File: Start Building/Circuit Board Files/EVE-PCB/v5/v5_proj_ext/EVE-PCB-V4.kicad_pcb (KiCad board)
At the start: 4 copper layers, 199.5 x 49.7 mm, 8 parts, among them J1 Conn_02x09_Top_Bottom, J2 Conn_02x09_Top_Bottom, J3 Conn_02x09_Top_Bottom, J4 Conn_02x09_Top_Bottom, J6 Conn_02x18_Odd_Even, J7 Conn_02x22_Odd_Even

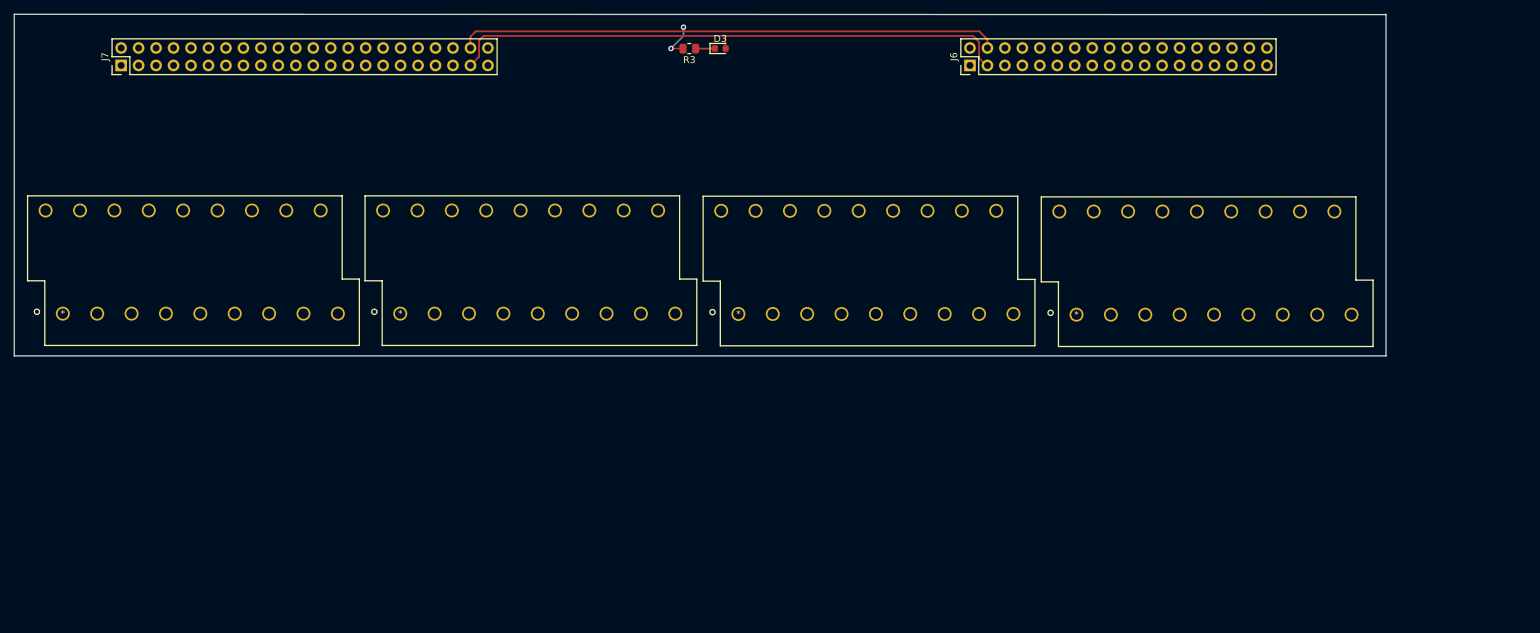
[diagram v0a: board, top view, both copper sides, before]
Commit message: PCBv5 update some schematics
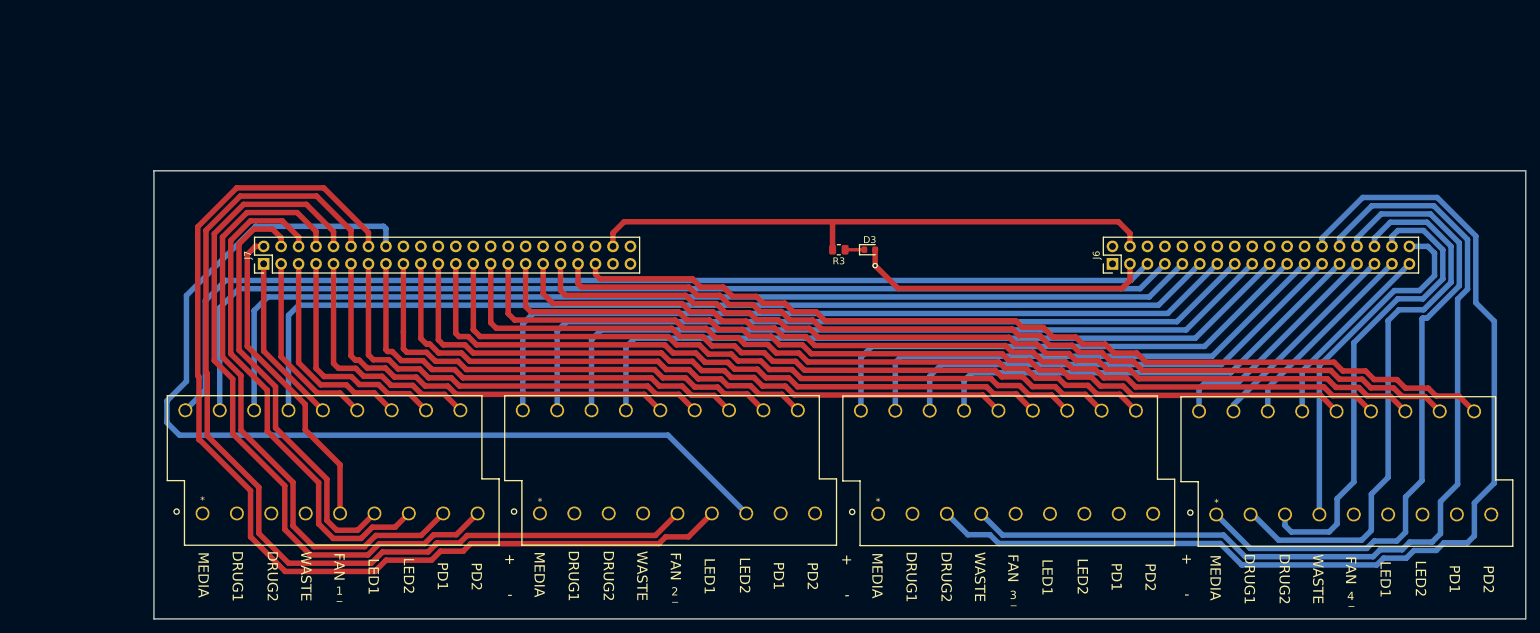
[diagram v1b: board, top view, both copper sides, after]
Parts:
- moved R3 36.5 mm to (150.0, 65.5)
- moved D3 36.5 mm to (154.5, 65.5)
- moved J7 35.5 mm to (66.4, 67.6)
- moved J6 35.5 mm to (189.8, 67.6)
- moved J2 35.5 mm to (155.8, 103.9)
- moved J3 35.5 mm to (106.6, 103.9)
- moved J1 35.5 mm to (57.5, 103.9)
- moved J4 35.5 mm to (204.9, 104.0)
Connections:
- J1 pad 1: /MEDIA1_POS -> /MEDIA1_NEG
- J1 pad 10: /MEDIA1_NEG -> /MEDIA1_POS
- J1 pad 11: /DRUG11_NEG -> /DRUG11_POS
- J1 pad 12: /DRUG12_NEG -> /DRUG12_POS
- J1 pad 13: /WASTE1_NEG -> /WASTE1_POS
- J1 pad 14: /FAN1_NEG -> /FAN1_POS
- J1 pad 15: /LED11_NEG -> /LED11_POS
- J1 pad 16: /LED12_NEG -> /LED12_POS
- J1 pad 17: /PD11_NEG -> /PD11_POS
- J1 pad 18: /PD12_NEG -> /PD12_POS
- J1 pad 2: /DRUG11_POS -> /DRUG11_NEG
- J1 pad 3: /DRUG12_POS -> /DRUG12_NEG
- J1 pad 4: /WASTE1_POS -> /WASTE1_NEG
- J1 pad 5: /FAN1_POS -> /FAN1_NEG
- J1 pad 6: /LED11_POS -> /LED11_NEG
- J1 pad 7: /LED12_POS -> /LED12_NEG
- J1 pad 8: /PD11_POS -> /PD11_NEG
- J1 pad 9: /PD12_POS -> /PD12_NEG
- J2 pad 1: /MEDIA3_POS -> /MEDIA3_NEG
- J2 pad 10: /MEDIA3_NEG -> /MEDIA3_POS
- J2 pad 11: /DRUG31_NEG -> /DRUG31_POS
- J2 pad 12: /DRUG32_NEG -> /DRUG32_POS
- J2 pad 13: /WASTE3_NEG -> /WASTE3_POS
- J2 pad 14: /FAN3_NEG -> /FAN3_POS
- J2 pad 15: /LED31_NEG -> /LED31_POS
- J2 pad 16: /LED32_NEG -> /LED32_POS
- J2 pad 17: /PD31_NEG -> /PD31_POS
- J2 pad 18: /PD32_NEG -> /PD32_POS
- J2 pad 2: /DRUG31_POS -> /DRUG31_NEG
- J2 pad 3: /DRUG32_POS -> /DRUG32_NEG
- J2 pad 4: /WASTE3_POS -> /WASTE3_NEG
- J2 pad 5: /FAN3_POS -> /FAN3_NEG
- J2 pad 6: /LED31_POS -> /LED31_NEG
- J2 pad 7: /LED32_POS -> /LED32_NEG
- J2 pad 8: /PD31_POS -> /PD31_NEG
- J2 pad 9: /PD32_POS -> /PD32_NEG
- J3 pad 1: /MEDIA2_POS -> /MEDIA2_NEG
- J3 pad 10: /MEDIA2_NEG -> /MEDIA2_POS
- J3 pad 11: /DRUG21_NEG -> /DRUG21_POS
- J3 pad 12: /DRUG22_NEG -> /DRUG22_POS
- J3 pad 13: /WASTE2_NEG -> /WASTE2_POS
- J3 pad 14: /FAN2_NEG -> /FAN2_POS
- J3 pad 15: /LED21_NEG -> /LED21_POS
- J3 pad 16: /LED22_NEG -> /LED22_POS
- J3 pad 17: /PD21_NEG -> /PD21_POS
- J3 pad 18: /PD22_NEG -> /PD22_POS
- J3 pad 2: /DRUG21_POS -> /DRUG21_NEG
- J3 pad 3: /DRUG22_POS -> /DRUG22_NEG
- J3 pad 4: /WASTE2_POS -> /WASTE2_NEG
- J3 pad 5: /FAN2_POS -> /FAN2_NEG
- J3 pad 6: /LED21_POS -> /LED21_NEG
- J3 pad 7: /LED22_POS -> /LED22_NEG
- J3 pad 8: /PD21_POS -> /PD21_NEG
- J3 pad 9: /PD22_POS -> /PD22_NEG
- J4 pad 1: /MEDIA4_POS -> /MEDIA4_NEG
- J4 pad 10: /MEDIA4_NEG -> /MEDIA4_POS
- J4 pad 11: /DRUG41_NEG -> /DRUG41_POS
- J4 pad 12: /DRUG42_NEG -> /DRUG42_POS
- J4 pad 13: /WASTE4_NEG -> /WASTE4_POS
- J4 pad 14: /FAN4_NEG -> /FAN4_POS
- J4 pad 15: /LED41_NEG -> /LED41_POS
- J4 pad 16: /LED42_NEG -> /LED42_POS
- J4 pad 17: /PD41_NEG -> /PD41_POS
- J4 pad 18: /PD42_NEG -> /PD42_POS
- J4 pad 2: /DRUG41_POS -> /DRUG41_NEG
- J4 pad 3: /DRUG42_POS -> /DRUG42_NEG
- J4 pad 4: /WASTE4_POS -> /WASTE4_NEG
- J4 pad 5: /FAN4_POS -> /FAN4_NEG
- J4 pad 6: /LED41_POS -> /LED41_NEG
- J4 pad 7: /LED42_POS -> /LED42_NEG
- J4 pad 8: /PD41_POS -> /PD41_NEG
- J4 pad 9: /PD42_POS -> /PD42_NEG
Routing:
- net /PD32_NEG: track 0.00 -> 239.9 mm
- net /PD31_NEG: track 0.00 -> 228.0 mm
- net /MEDIA2_NEG: track 0.00 -> 224.1 mm
- net /LED32_NEG: track 0.00 -> 216.2 mm
- net /DRUG21_NEG: track 0.00 -> 212.6 mm
- net /LED31_NEG: track 0.00 -> 203.8 mm
- net /DRUG22_NEG: track 0.00 -> 200.7 mm
- net /FAN3_NEG: track 0.00 -> 191.9 mm
- net /WASTE2_NEG: track 0.00 -> 188.4 mm
- net /MEDIA1_NEG: track 0.00 -> 182.5 mm
- net /PD42_NEG: track 0.00 -> 180.5 mm
- net /DRUG11_NEG: track 0.00 -> 177.3 mm
- net /DRUG12_NEG: track 0.00 -> 175.0 mm
- net /PD41_NEG: track 0.00 -> 174.7 mm
- net /LED42_NEG: track 0.00 -> 173.0 mm
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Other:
- board size 199.5 x 49.7 mm -> 199.5 x 65.2 mm
- net class vref: clearance 0.3 -> 0.4; trace_width 0.7 -> 0.8
- board text added: "+"
- board text added: "-"
- board text added: "1"
- board text added: "2"
- board text added: "3"
- board text added: "4"
- board text added: "DRUG1"
- board text added: "DRUG2"
- board text added: "FAN"
- board text added: "LED1"
- board text added: "LED2"
- board text added: "MEDIA"
- board text added: "PD1"
- board text added: "PD2"
- board text added: "WASTE"
- board text added: "_"

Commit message: Updates to PCB v5
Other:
- board text added: "Adapter Board"
- board text added: "Designed by Vishhvaan"
- board text added: "EVE"
- board text added: "JLCJLCJLCJLC"
